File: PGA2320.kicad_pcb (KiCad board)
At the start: 2 copper layers, 50 x 50 mm, 20 parts, among them J1 XH2.54-3P, J2 XH2.54-3P, J3 2P-2.54, J4 3P-2.54, P1 SDO_TO_OTHER_PGA2311, P2 CONTROLLER, U1 PGA2320

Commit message: pcb layout
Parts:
- P1: footprint Connector_Pin:Pin_D0.7mm_L6.5mm_W1.8mm_FlatFork -> Connector_Pin:Pin_D0.9mm_L10.0mm_W2.4mm_FlatFork
- moved R3 39.6 mm to (162.8, 77.7)
- moved R2 35.3 mm to (162.8, 90.7), turned to 180 degrees
- moved C2 33.1 mm to (117.9, 84.1), turned to 90 degrees
- moved JP1 28.3 mm to (146.2, 95.6), turned to 180 degrees
- moved J3 27.7 mm to (135.6, 61.2), turned to 90 degrees
- moved D1 26.6 mm to (122.4, 86.6)
- moved C1 26.6 mm to (127.5, 86.6)
- moved J2 25.7 mm to (157.0, 104.9), turned to 180 degrees
- moved D3 25.6 mm to (162.8, 73.9), turned to 180 degrees
- moved J4 25.2 mm to (162.8, 86.6), turned to 90 degrees
- moved P1 24.2 mm to (119.1, 64.0)
- moved P2 24.1 mm to (126.7, 64.0)
- moved J1 21.5 mm to (152.0, 61.7)
- moved D2 14.1 mm to (162.8, 94.2)
- moved U1 11.0 mm to (141.4, 83.6)
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
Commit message: pcb layout
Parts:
- moved C4 5.46 mm to (148.6, 85.9), turned to 90 degrees
- moved C3 5.34 mm to (148.6, 81.5), turned to 90 degrees
- moved C5 2.08 mm to (154.2, 81.3), turned to 180 degrees
- moved C6 1.71 mm to (154.2, 86.2)
- moved J4 0.51 mm to (162.3, 86.6)
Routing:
- net +15V: track 0.00 -> 22.7 mm
- net -15V: track 0.00 -> 17.7 mm
- net GND_A: track 0.00 -> 11.7 mm
- net Net-(D2-A): track 0.00 -> 3.70 mm
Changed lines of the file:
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@@
   )
   (footprint "Audio_Module:c_0805" (layer "F.Cu")
-    (at 153.87574 82.296)
+    (at 148.59 81.51876 90)
     (descr "SMT capacitor, 0805")
     (property "Sheetfile" "PGA2320.kicad_sch")
@@
     (property "notes" "ceramic or metal film")
     (attr through_hole)
-    (fp_text reference "C3" (at 0 -0.9906) (layer "F.SilkS")
+    (fp_text reference "C3" (at 0 -0.9906 90) (layer "F.SilkS")
         (effects (font (size 0.29972 0.29972) (thickness 0.06096)))
     )
-    (fp_text value "0.1uF" (at 0 0.9906) (layer "F.SilkS") hide
+    (fp_text value "0.1uF" (at 0 0.9906 90) (layer "F.SilkS") hide
         (effects (font (size 0.29972 0.29972) (thickness 0.06096)))
     )
@@
     (fp_line (start 1.016 0.635) (end -1.016 0.635)
       (stroke (width 0.127) (type solid)) (layer "F.SilkS"))
-    (pad "1" smd rect (at 0.9525 0) (size 1.30048 1.4986) (layers "F.Cu" "F.Paste" "F.Mask")
+    (pad "1" smd rect (at 0.9525 0 90) (size 1.30048 1.4986) (layers "F.Cu" "F.Paste" "F.Mask")
       (net 3 "GND_A") (pintype "passive"))
-    (pad "2" smd rect (at -0.9525 0) (size 1.30048 1.4986) (layers "F.Cu" "F.Paste" "F.Mask")
+    (pad "2" smd rect (at -0.9525 0 90) (size 1.30048 1.4986) (layers "F.Cu" "F.Paste" "F.Mask")
       (net 4 "-15V") (pintype "passive"))
     (model "walter/smd_cap/c_0805.wrl"
@@
   )
   (footprint "Audio_Module:c_0805" (layer "F.Cu")
-    (at 153.87574 84.582)
+    (at 148.59 85.9405 90)
     (descr "SMT capacitor, 0805")
     (property "Sheetfile" "PGA2320.kicad_sch")
@@
     (property "notes" "ceramic or metal film")
     (attr through_hole)
-    (fp_text reference "C4" (at 0 -0.9906) (layer "F.SilkS")
+    (fp_text reference "C4" (at 0 -0.9906 90) (layer "F.SilkS")
         (effects (font (size 0.29972 0.29972) (thickness 0.06096)))
     )
-    (fp_text value "0.1uF" (at 0 0.9906) (layer "F.SilkS") hide
+    (fp_text value "0.1uF" (at 0 0.9906 90) (layer "F.SilkS") hide
         (effects (font (size 0.29972 0.29972) (thickness 0.06096)))
     )
@@
     (fp_line (start 1.016 0.635) (end -1.016 0.635)
       (stroke (width 0.127) (type solid)) (layer "F.SilkS"))
-    (pad "1" smd rect (at 0.9525 0) (size 1.30048 1.4986) (layers "F.Cu" "F.Paste" "F.Mask")
+    (pad "1" smd rect (at 0.9525 0 90) (size 1.30048 1.4986) (layers "F.Cu" "F.Paste" "F.Mask")
       (net 5 "+15V") (pintype "passive"))
-    (pad "2" smd rect (at -0.9525 0) (size 1.30048 1.4986) (layers "F.Cu" "F.Paste" "F.Mask")
+    (pad "2" smd rect (at -0.9525 0 90) (size 1.30048 1.4986) (layers "F.Cu" "F.Paste" "F.Mask")
       (net 3 "GND_A") (pintype "passive"))
     (model "walter/smd_cap/c_0805.wrl"
@@
   )
   (footprint "Audio_Module:c_tant_C" (layer "F.Cu")
-    (at 153.68524 79.248)
+    (at 154.178 81.26476 180)
     (descr "SMT capacitor, tantalum size C")
     (property "Sheetfile" "PGA2320.kicad_sch")
@@
     (fp_line (start 3.048 1.5875) (end 3.048 -1.5875)
       (stroke (width 0.127) (type solid)) (layer "F.SilkS"))
-    (pad "1" smd rect (at 2.52476 0) (size 2.55016 2.49936) (layers "F.Cu" "F.Paste" "F.Mask")
+    (pad "1" smd rect (at 2.52476 0 180) (size 2.55016 2.49936) (layers "F.Cu" "F.Paste" "F.Mask")
       (net 3 "GND_A") (pintype "passive"))
-    (pad "2" smd rect (at -2.52476 0) (size 2.55016 2.49936) (layers "F.Cu" "F.Paste" "F.Mask")
+    (pad "2" smd rect (at -2.52476 0 180) (size 2.55016 2.49936) (layers "F.Cu" "F.Paste" "F.Mask")
       (net 4 "-15V") (pintype "passive"))
     (model "walter/smd_cap/c_tant_C.wrl"
@@
   )
   (footprint "digikey-footprints:PinHeader_1x3_P2.54mm_Drill1.02mm" (layer "F.Cu")
-    (at 162.814 86.614 90)
+    (at 162.306 86.609 90)
     (descr "http://www.molex.com/pdm_docs/sd/022232031_sd.pdf")
     (property "Category" "Connectors, Interconnects")
@@
   )
   (footprint "Audio_Module:c_tant_C" (layer "F.Cu")
-    (at 153.93924 87.884)
+    (at 154.178 86.1945)
     (descr "SMT capacitor, tantalum size C")
     (property "Sheetfile" "PGA2320.kicad_sch")
@@
   (gr_rect (start 162.56 97.79) (end 162.56 97.79)
     (stroke (width 0.1) (type default)) (fill none) (layer "Edge.Cuts"))
+  (segment (start 148.565 86.868) (end 148.59 86.893) (width 0.25) (layer "F.Cu") (net 3))
+  (segment (start 150.95474 80.56626) (end 151.65324 81.26476) (width 0.25) (layer "F.Cu") (net 3))
+  (segment (start 146.19552 86.868) (end 148.565 86.868) (width 0.25) (layer "F.Cu") (net 3))
+  (segment (start 148.184 80.16026) (end 148.59 80.56626) (width 0.25) (layer "F.Cu") (net 3))
+  (segment (start 146.19552 80.4295) (end 148.184 80.4295) (width 0.25) (layer "F.Cu") (net 3))
+  (segment (start 148.59 86.893) (end 150.95474 86.893) (width 0.25) (layer "F.Cu") (net 3))
+  (segment (start 148.59 80.56626) (end 150.95474 80.56626) (width 0.25) (layer "F.Cu") (net 3))
+  (segment (start 150.95474 86.893) (end 151.65324 86.1945) (width 0.25) (layer "F.Cu") (net 3))
+  (segment (start 146.19552 82.9695) (end 148.361 82.9695) (width 0.25) (layer "F.Cu") (net 4))
+  (segment (start 148.59 82.47126) (end 149.4155 83.29676) (width 0.25) (layer "F.Cu") (net 4))
+  (segment (start 148.361 82.70026) (end 148.59 82.47126) (width 0.25) (layer "F.Cu") (net 4))
+  (segment (start 155.194 83.29676) (end 156.70276 81.788) (width 0.25) (layer "F.Cu") (net 4))
+  (segment (start 156.70276 81.788) (end 156.70276 81.26476) (width 0.25) (layer "F.Cu") (net 4))
+  (segment (start 156.70276 81.534) (end 162.301 81.534) (width 0.25) (layer "F.Cu") (net 4))
+  (segment (start 162.301 81.534) (end 162.306 81.529) (width 0.25) (layer "F.Cu") (net 4))
+  (segment (start 149.4155 83.29676) (end 155.194 83.29676) (width 0.25) (layer "F.Cu") (net 4))
+  (segment (start 162.306 89.789) (end 161.417 90.678) (width 0.25) (layer "F.Cu") (net 5))
+  (segment (start 149.4155 84.1625) (end 155.194 84.1625) (width 0.25) (layer "F.Cu") (net 5))
+  (segment (start 162.306 86.609) (end 162.306 89.789) (width 0.25) (layer "F.Cu") (net 5))
+  (segment (start 156.464 85.4325) (end 156.464 86.1945) (width 0.25) (layer "F.Cu") (net 5))
+  (segment (start 147.93 84.328) (end 148.59 84.988) (width 0.25) (layer "F.Cu") (net 5))
+  (segment (start 146.19552 84.328) (end 147.93 84.328) (width 0.25) (layer "F.Cu") (net 5))
+  (segment (start 161.803 86.106) (end 162.306 86.609) (width 0.25) (layer "F.Cu") (net 5))
+  (segment (start 156.464 86.1945) (end 161.803 86.1945) (width 0.25) (layer "F.Cu") (net 5))
+  (segment (start 155.194 84.1625) (end 156.464 85.4325) (width 0.25) (layer "F.Cu") (net 5))
+  (segment (start 148.59 84.988) (end 149.4155 84.1625) (width 0.25) (layer "F.Cu") (net 5))
+  (segment (start 164.211 93.88348) (end 164.56152 94.234) (width 0.25) (layer "F.Cu") (net 7))
+  (segment (start 164.211 90.678) (end 164.211 93.88348) (width 0.25) (layer "F.Cu") (net 7))
 )

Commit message: pcb layout
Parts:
- added ?: , , F.Cu at (118.4, 105.4)
- added ?: , , F.Cu at (118.6, 61.2)
- added ?: , , F.Cu at (163.1, 105.9)
- added REF**: MountingHole_3.5mm_Pad, MountingHole:MountingHole_3.5mm_Pad, F.Cu at (163.1, 61.7)
- moved J3 28.1 mm to (117.6, 82.8), turned to 0 degrees
- moved C2 8.97 mm to (126.8, 84.1)
- moved J2 5.33 mm to (151.6, 104.9), turned to 0 degrees
- moved J1 4.97 mm to (157.0, 61.7), turned to 180 degrees
- moved P2 4.65 mm to (130.3, 61.0)
- moved P1 4.65 mm to (122.7, 61.0)
- moved C1 3.47 mm to (129.9, 84.1), turned to 90 degrees
- moved C5 0.81 mm to (155.0, 81.0)
- moved C6 0.79 mm to (155.0, 86.4)
- moved D1 0.55 mm to (122.2, 86.1)
- moved C3 0.52 mm to (149.1, 81.5)
- moved C4 0.52 mm to (149.1, 85.9)
- moved R1 0.26 mm to (122.2, 83.3)
- moved J4 0.25 mm to (162.6, 86.6)
- moved R2 0.25 mm to (162.6, 90.7)
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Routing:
- net VIN_R: track 0.00 -> 31.7 mm
- net VOUT_L: track 0.00 -> 26.7 mm, vias 0 -> 1
- net VOUT_R: track 0.00 -> 24.5 mm
- net +5VD: track 0.00 -> 22.2 mm
- net VIN_L: track 0.00 -> 21.9 mm
- net -15V: track 17.7 -> 27.6 mm
- net Net-(D3-A): track 0.00 -> 3.96 mm
- net Net-(D1-A): track 0.00 -> 2.94 mm
- net GND_A: track 11.7 -> 8.82 mm, vias 0 -> 2
- added copper zone on F.Cu, net GND_A
- added copper zone on F.Cu, net GND_D

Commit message: layout
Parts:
- C1, C2, C3, C4, C5, C6: moved to B.Cu
- moved D3 32.3 mm to (154.7, 105.2), turned to -90 degrees
- moved R3 28.1 mm to (157.7, 105.4), turned to 90 degrees
- moved D2 26.6 mm to (138.7, 105.4), turned to -90 degrees
- moved J3 25.6 mm to (126.7, 106.7), turned to 90 degrees
- moved R2 25.4 mm to (141.7, 105.2), turned to 90 degrees
- moved J4 25.0 mm to (145.8, 105.2), turned to 0 degrees
- moved J2 22.8 mm to (162.8, 85.1), turned to -90 degrees
- moved R1 19.4 mm to (127.3, 102.1), turned to 90 degrees
- moved C3 19.0 mm to (155.0, 99.6), turned to 0 degrees
- moved D1 17.8 mm to (130.1, 102.1), turned to 90 degrees
- moved J1 15.6 mm to (162.8, 76.2), turned to -90 degrees
- moved C4 13.7 mm to (150.6, 99.6), turned to 0 degrees
- moved C2 13.4 mm to (128.0, 97.5), turned to 0 degrees
- moved C5 12.7 mm to (155.5, 93.7), turned to -90 degrees
- moved C1 10.5 mm to (128.0, 94.4), turned to 0 degrees
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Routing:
- net VIN_R: track 31.7 -> 21.4 mm, vias 0 -> 1
- net VOUT_L: track 26.7 -> 18.4 mm
- net +15V: track 22.7 -> 30.2 mm, vias 0 -> 2
- net +5VD: track 22.2 -> 16.6 mm
- net VOUT_R: track 24.5 -> 19.3 mm, vias 0 -> 1
- net -15V: track 27.6 -> 32.0 mm, vias 0 -> 2
- net VIN_L: track 21.9 -> 17.6 mm, vias 0 -> 1
- net Net-(D3-A): track 3.96 -> 0.00 mm
- net GND_A: track 8.82 -> 7.81 mm, vias 2 -> 0
- removed copper zone on F.Cu, net GND_A
- removed copper zone on F.Cu, net GND_D

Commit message: layout
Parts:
- D1, D2, D3: footprint Audio_Module:Led_1206 -> LED_SMD:LED_0805_2012Metric_Pad1.15x1.40mm_HandSolder
- R1, R2, R3: footprint Audio_Module:r_1210 -> Resistor_SMD:R_0805_2012Metric_Pad1.20x1.40mm_HandSolder
- moved J3 46.6 mm to (129.5, 60.2)
- moved R2 44.6 mm to (144.8, 60.7), turned to 180 degrees
- moved D3 44.5 mm to (157.5, 60.7), turned to 0 degrees
- moved J4 43.5 mm to (148.6, 61.7)
- moved D2 42.9 mm to (144.8, 63.0), turned to 180 degrees
- moved R3 42.7 mm to (157.5, 62.7), turned to 0 degrees
- moved R1 42.7 mm to (125.5, 59.4), turned to 0 degrees
- moved D1 40.8 mm to (125.5, 61.5), turned to 180 degrees
- moved C3 19.0 mm to (149.1, 81.5), turned to 90 degrees
- moved P1 18.5 mm to (137.4, 72.4), turned to 90 degrees
- moved C4 14.3 mm to (149.1, 85.3), turned to 90 degrees
- moved C2 13.6 mm to (130.3, 84.1), turned to 90 degrees
- moved C5 12.2 mm to (154.4, 81.5), turned to 0 degrees
- moved C1 12.2 mm to (133.6, 83.6), turned to 90 degrees
- moved C6 9.39 mm to (154.4, 85.3), turned to 180 degrees
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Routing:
- net MUTE: track 0.00 -> 31.2 mm
- net SCLK: track 0.00 -> 26.4 mm
- net SDI: track 0.00 -> 19.5 mm
- net +5VD: track 16.6 -> 32.2 mm, vias 0 -> 1
- net CS: track 0.00 -> 15.6 mm
- net ZCEN: track 0.00 -> 12.4 mm
- net GND_D: track 0.00 -> 6.13 mm, vias 0 -> 1
- net GND_A: track 7.81 -> 2.84 mm, vias 0 -> 2
- net -15V: track 32.0 -> 28.4 mm
- net Net-(D3-A): track 0.00 -> 2.04 mm
- net Net-(D2-A): track 3.70 -> 2.29 mm
- net Net-(D1-A): track 2.94 -> 2.04 mm
- net VIN_R: track 21.4 -> 22.3 mm
- added copper zone on B.Cu, net GND_A
- added copper zone on F.Cu, net GND_A
- added copper zone on B.Cu, net GND_D
- added copper zone on F.Cu, net GND_D

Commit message: finish first version
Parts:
- removed REF**: MountingHole_3.5mm_Pad, MountingHole:MountingHole_3.5mm_Pad
- added ?: , , F.Cu at (163.1, 61.2)
- P1: value SDO_TO_OTHER_PGA2311 -> SDO
- moved D3 0.25 mm to (157.2, 60.7)
- moved R3 0.25 mm to (157.2, 62.7)
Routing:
- net SDO: track 0.00 -> 16.6 mm, vias 0 -> 1
- net +15V: track 30.0 -> 32.7 mm
- net SCLK: track 26.4 -> 24.4 mm, vias 0 -> 1
- net MUTE: track 31.2 -> 29.6 mm, vias 0 -> 1
- net -15V: track 28.4 -> 29.5 mm
- net VIN_R: track 22.3 -> 21.2 mm
- net SDI: track 19.5 -> 20.0 mm, vias 0 -> 1
- net VOUT_L: track 18.4 -> 17.8 mm
- net CS: track 15.6 -> 15.9 mm, vias 0 -> 1
- net ZCEN: track 12.4 -> 12.0 mm, vias 0 -> 1

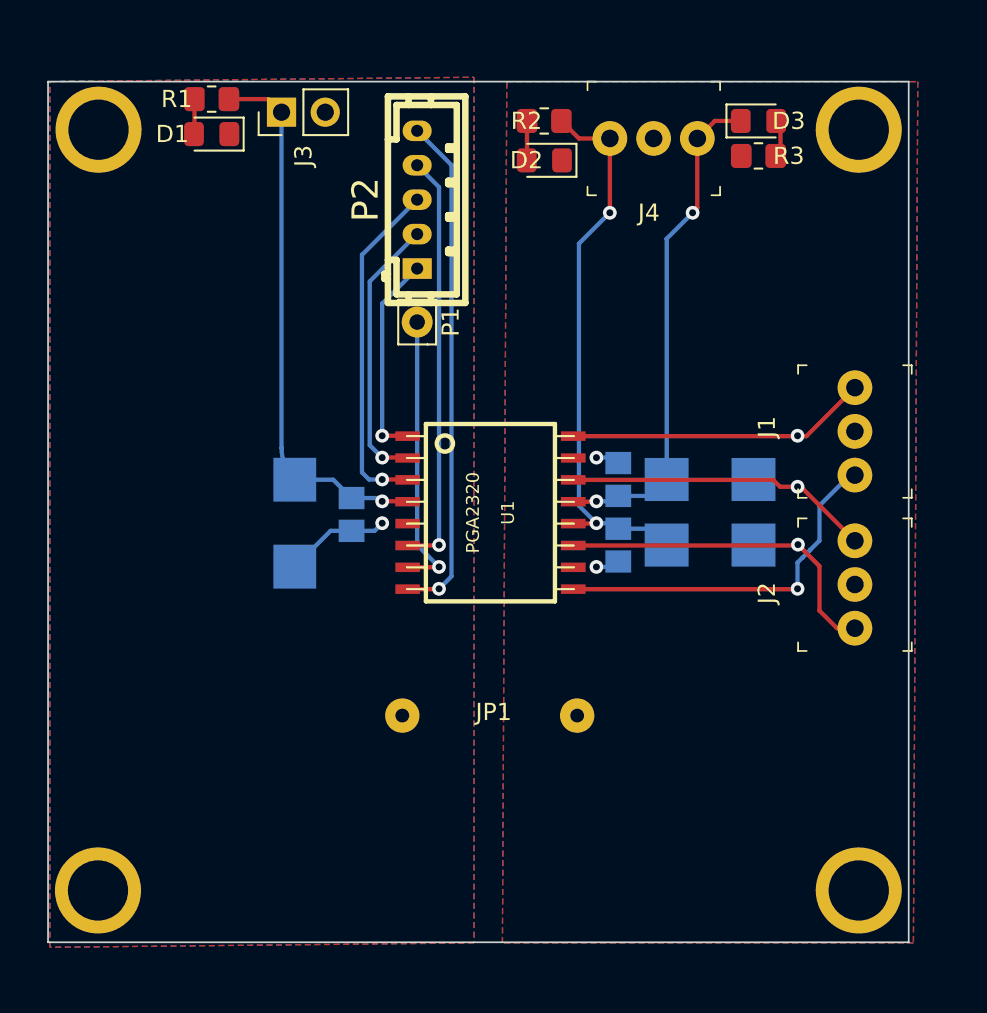
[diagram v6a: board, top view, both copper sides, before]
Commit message: improve silk screen
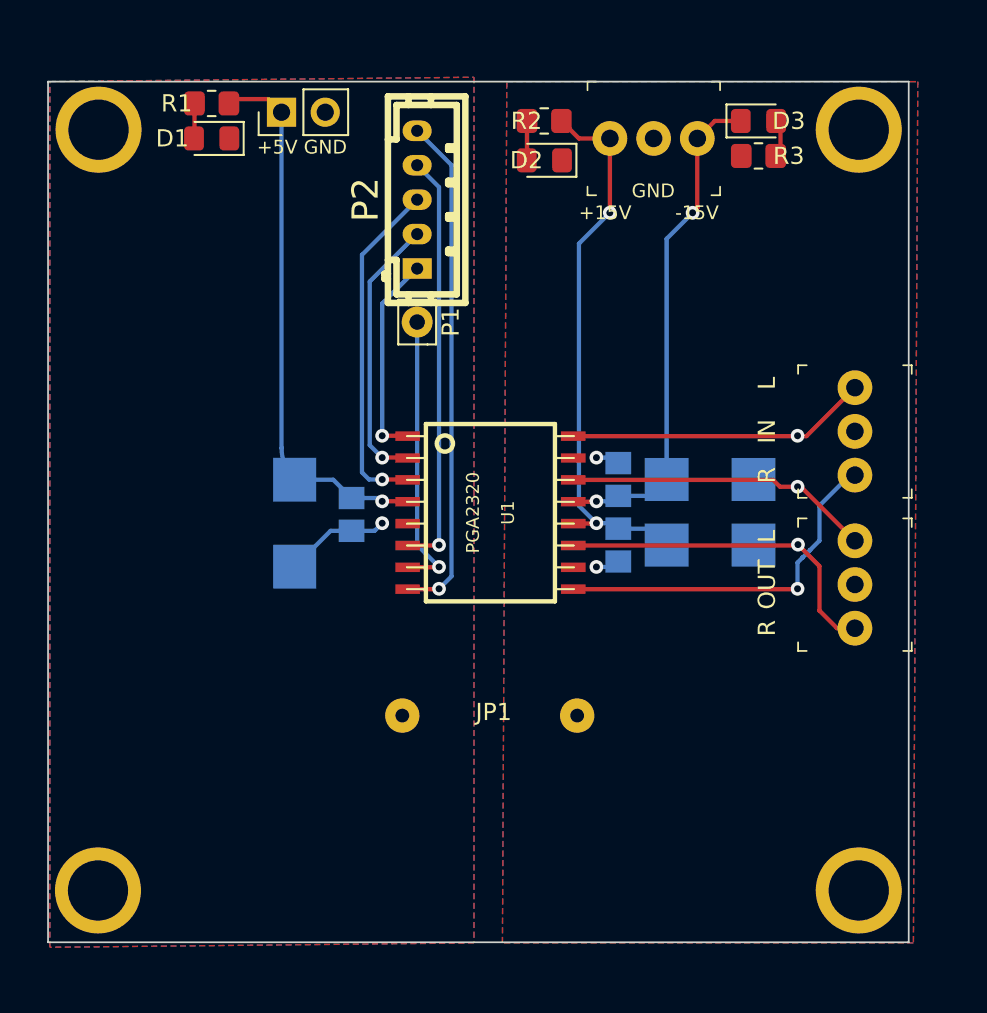
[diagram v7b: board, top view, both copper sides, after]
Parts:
- moved D1 0.25 mm to (125.5, 61.7)
- moved R1 0.25 mm to (125.5, 59.7)
- renumbered J1 to IN, J2 to OUT
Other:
- board text added: "+15V"
- board text added: "+5V"
- board text added: "-15V"
- board text added: "GND"
- board text added: "L"
- board text added: "R"
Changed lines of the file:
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@@
     (property "ki_keywords" "screw terminal")
     (attr through_hole)
-    (fp_text reference "J3" (at -2.54 1.275 90) (layer "F.SilkS")
+    (fp_text reference "J3" (at -2.54 1.275 90) (layer "F.SilkS") hide
         (effects (font (size 1 1) (thickness 0.15)))
     )
@@
     (property "ki_keywords" "WM4201-ND KK 6373")
     (attr through_hole)
-    (fp_text reference "J2" (at 3.043 5.111513 90) (layer "F.SilkS")
+    (fp_text reference "OUT" (at 2.535 5.111513 90) (layer "F.SilkS")
         (effects (font (size 1 1) (thickness 0.15)))
     )
@@
     (property "ki_keywords" "WM4201-ND KK 6373")
     (attr through_hole)
-    (fp_text reference "J1" (at 2.286 5.111513 -270) (layer "F.SilkS")
+    (fp_text reference "IN" (at 2.54 5.111513 90) (layer "F.SilkS")
         (effects (font (size 1 1) (thickness 0.15)))
     )
@@
   )
   (footprint "Resistor_SMD:R_0805_2012Metric_Pad1.20x1.40mm_HandSolder" (layer "F.Cu")
-    (at 125.476 59.436)
+    (at 125.476 59.69)
     (descr "Resistor SMD 0805 (2012 Metric), square (rectangular) end terminal, IPC_7351 nominal with elongated pad for handsoldering. (Body size source: IPC-SM-782 page 72, https://www.pcb-3d.com/wordpress/wp-content/uploads/ipc-sm-782a_amendment_1_and_2.pdf), generated with kicad-footprint-generator")
     (tags "resistor handsolder")
@@
   )
   (footprint "LED_SMD:LED_0805_2012Metric_Pad1.15x1.40mm_HandSolder" (layer "F.Cu")
-    (at 125.476 61.468 180)
+    (at 125.476 61.722 180)
     (descr "LED SMD 0805 (2012 Metric), square (rectangular) end terminal, IPC_7351 nominal, (Body size source: https://docs.google.com/spreadsheets/d/1BsfQQcO9C6DZCsRaXUlFlo91Tg2WpOkGARC1WS5S8t0/edit?usp=sharing), generated with kicad-footprint-generator")
     (tags "LED handsolder")
@@
     (property "ki_keywords" "screw terminal")
     (attr through_hole)
-    (fp_text reference "J4" (at 2.265 4.318) (layer "F.SilkS")
+    (fp_text reference "J4" (at 2.265 4.318) (layer "F.SilkS") hide
         (effects (font (size 1 1) (thickness 0.15)))
     )
@@
   (gr_rect (start 162.56 97.79) (end 162.56 97.79)
     (stroke (width 0.1) (type default)) (fill none) (layer "Edge.Cuts"))
+  (gr_text "R" (at 157.734 90.17 90) (layer "F.SilkS")
+    (effects (font (size 1 1) (thickness 0.15)))
+  )
+  (gr_text "+5V" (at 129.286 62.23) (layer "F.SilkS")
+    (effects (font (size 0.8 0.8) (thickness 0.15)))
+  )
+  (gr_text "GND" (at 151.13 64.77) (layer "F.SilkS")
+    (effects (font (size 0.8 0.8) (thickness 0.15)))
+  )
+  (gr_text "L" (at 157.734 84.836 90) (layer "F.SilkS")
+    (effects (font (size 1 1) (thickness 0.15)))
+  )
+  (gr_text "+15V" (at 148.336 66.04) (layer "F.SilkS")
+    (effects (font (size 0.8 0.8) (thickness 0.15)))
+  )
+  (gr_text "R" (at 157.734 81.28 90) (layer "F.SilkS")
+    (effects (font (size 1 1) (thickness 0.15)))
+  )
+  (gr_text "L" (at 157.734 75.946 90) (layer "F.SilkS")
+    (effects (font (size 1 1) (thickness 0.15)))
+  )
+  (gr_text "GND" (at 132.08 62.23) (layer "F.SilkS")
+    (effects (font (size 0.8 0.8) (thickness 0.15)))
+  )
+  (gr_text "-15V" (at 153.67 66.04) (layer "F.SilkS")
+    (effects (font (size 0.8 0.8) (thickness 0.15)))
+  )
   (segment (start 136.835696 82.804) (end 136.859513 82.827817) (width 0.25) (layer "F.Cu") (net 1))
   (segment (start 128.773 59.436) (end 129.535 60.198) (width 0.25) (layer "F.Cu") (net 1))
